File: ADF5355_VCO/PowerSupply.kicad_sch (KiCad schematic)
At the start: 14 parts, among them IC1 ADM7150ACPZ-3.3-R7, IC2 ADM7150ARDZ-5.0, J1 Conn_01x02, SW1 SW_SPST

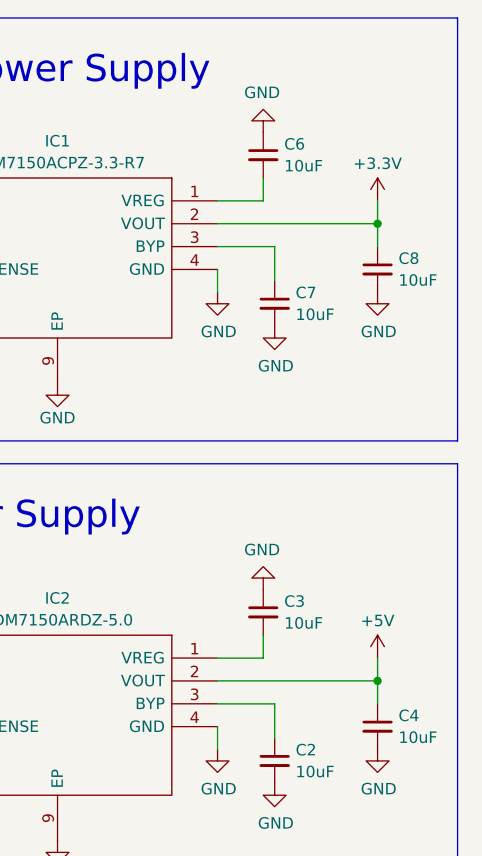
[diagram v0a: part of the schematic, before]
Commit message: Moved power ports to the main sheet
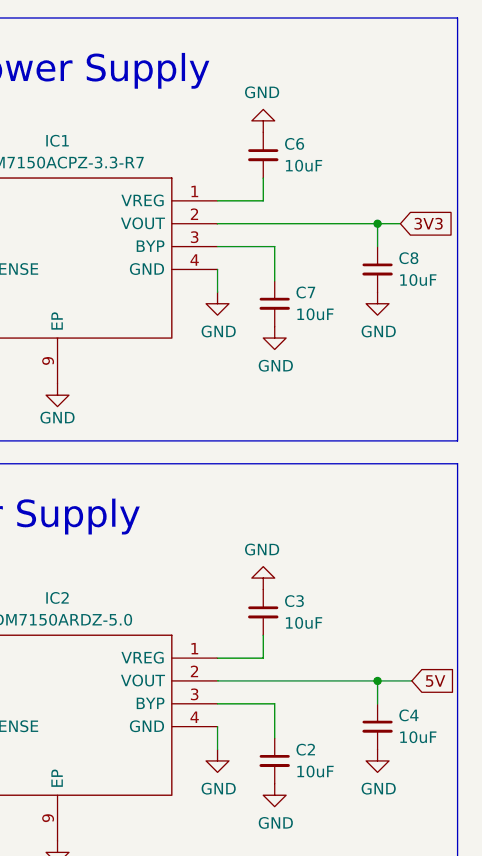
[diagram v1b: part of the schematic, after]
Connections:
- net +3.3V renamed 3V3
- net +5V renamed 5V
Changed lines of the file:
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@@
-    (stroke (width 0) (type default))
-  )
-  (wire (pts (xy 154.94 113.03) (xy 154.94 115.57))
     (stroke (width 0) (type default))
   )
@@
     (stroke (width 0) (type default))
   )
+  (wire (pts (xy 154.94 115.57) (xy 158.75 115.57))
+    (stroke (width 0) (type default))
+  )
+  (wire (pts (xy 154.94 64.77) (xy 157.48 64.77))
+    (stroke (width 0) (type default))
+  )
   (wire (pts (xy 137.16 62.23) (xy 142.24 62.23))
     (stroke (width 0) (type default))
@@
     (stroke (width 0) (type default))
   )
+  (wire (pts (xy 154.94 64.77) (xy 154.94 67.31))
+    (stroke (width 0) (type default))
+  )
   (wire (pts (xy 87.63 110.49) (xy 87.63 113.03))
     (stroke (width 0) (type default))
@@
   )
   (wire (pts (xy 101.6 120.65) (xy 95.25 120.65))
-    (stroke (width 0) (type default))
-  )
-  (wire (pts (xy 154.94 62.23) (xy 154.94 64.77))
-    (stroke (width 0) (type default))
-  )
-  (wire (pts (xy 154.94 64.77) (xy 154.94 67.31))
     (stroke (width 0) (type default))
   )
@@
   (text "External power" (at 39.37 77.47 0)
     (effects (font (size 3 3)) (justify left bottom))
+  )
+  (global_label "5V" (shape input) (at 158.75 115.57 0) (fields_autoplaced)
+    (effects (font (size 1.27 1.27)) (justify left))
+    (property "Intersheetrefs" "${INTERSHEET_REFS}" (at 163.2997 115.57 0)
+      (effects (font (size 1.27 1.27)) (justify left) hide)
+    )
+  )
+  (global_label "3V3" (shape input) (at 157.48 64.77 0) (fields_autoplaced)
+    (effects (font (size 1.27 1.27)) (justify left))
+    (property "Intersheetrefs" "${INTERSHEET_REFS}" (at 163.2392 64.77 0)
+      (effects (font (size 1.27 1.27)) (justify left) hide)
+    )
   )
   (global_label "DC_EN" (shape input) (at 101.6 64.77 180) (fields_autoplaced)
@@
         (path "/29349b68-071c-451b-9b1e-10b5ef7e12a6/00000000-0000-0000-0000-000064ac72b7"
           (reference "C7") (unit 1)
-        )
-      )
-    )
-  )
-  (symbol (lib_id "power:+5V") (at 154.94 113.03 0) (unit 1)
-    (in_bom yes) (on_board yes) (dnp no) (fields_autoplaced)
-    (property "Reference" "#PWR010" (at 154.94 116.84 0)
-      (effects (font (size 1.27 1.27)) hide)
-    )
-    (property "Value" "+5V" (at 154.94 108.8969 0)
-      (effects (font (size 1.27 1.27)))
-    )
-    (property "Footprint" "" (at 154.94 113.03 0)
-      (effects (font (size 1.27 1.27)) hide)
-    )
-    (property "Datasheet" "" (at 154.94 113.03 0)
-      (effects (font (size 1.27 1.27)) hide)
-    )
-    (pin "1")
-    (instances
-      (project "ADF5355_VCO"
-        (path "/29349b68-071c-451b-9b1e-10b5ef7e12a6/00000000-0000-0000-0000-000064ac72b7"
-          (reference "#PWR010") (unit 1)
         )
       )
@@
         )
       )
-    )
-  )
-  (symbol (lib_id "power:+3.3V") (at 154.94 62.23 0) (unit 1)
-    (in_bom yes) (on_board yes) (dnp no) (fields_autoplaced)
-    (property "Reference" "#PWR09" (at 154.94 66.04 0)
-      (effects (font (size 1.27 1.27)) hide)
-    )
-    (property "Value" "+3.3V" (at 154.94 58.0969 0)
-      (effects (font (size 1.27 1.27)))
-    )
-    (property "Footprint" "" (at 154.94 62.23 0)
-      (effects (font (size 1.27 1.27)) hide)
-    )
-    (property "Datasheet" "" (at 154.94 62.23 0)
-      (effects (font (size 1.27 1.27)) hide)
-    )
-    (pin "1")
-    (instances
-      (project "ADF5355_VCO"
-        (path "/29349b68-071c-451b-9b1e-10b5ef7e12a6/00000000-0000-0000-0000-000064ac72b7"
-          (reference "#PWR09") (unit 1)
-        )
-      )

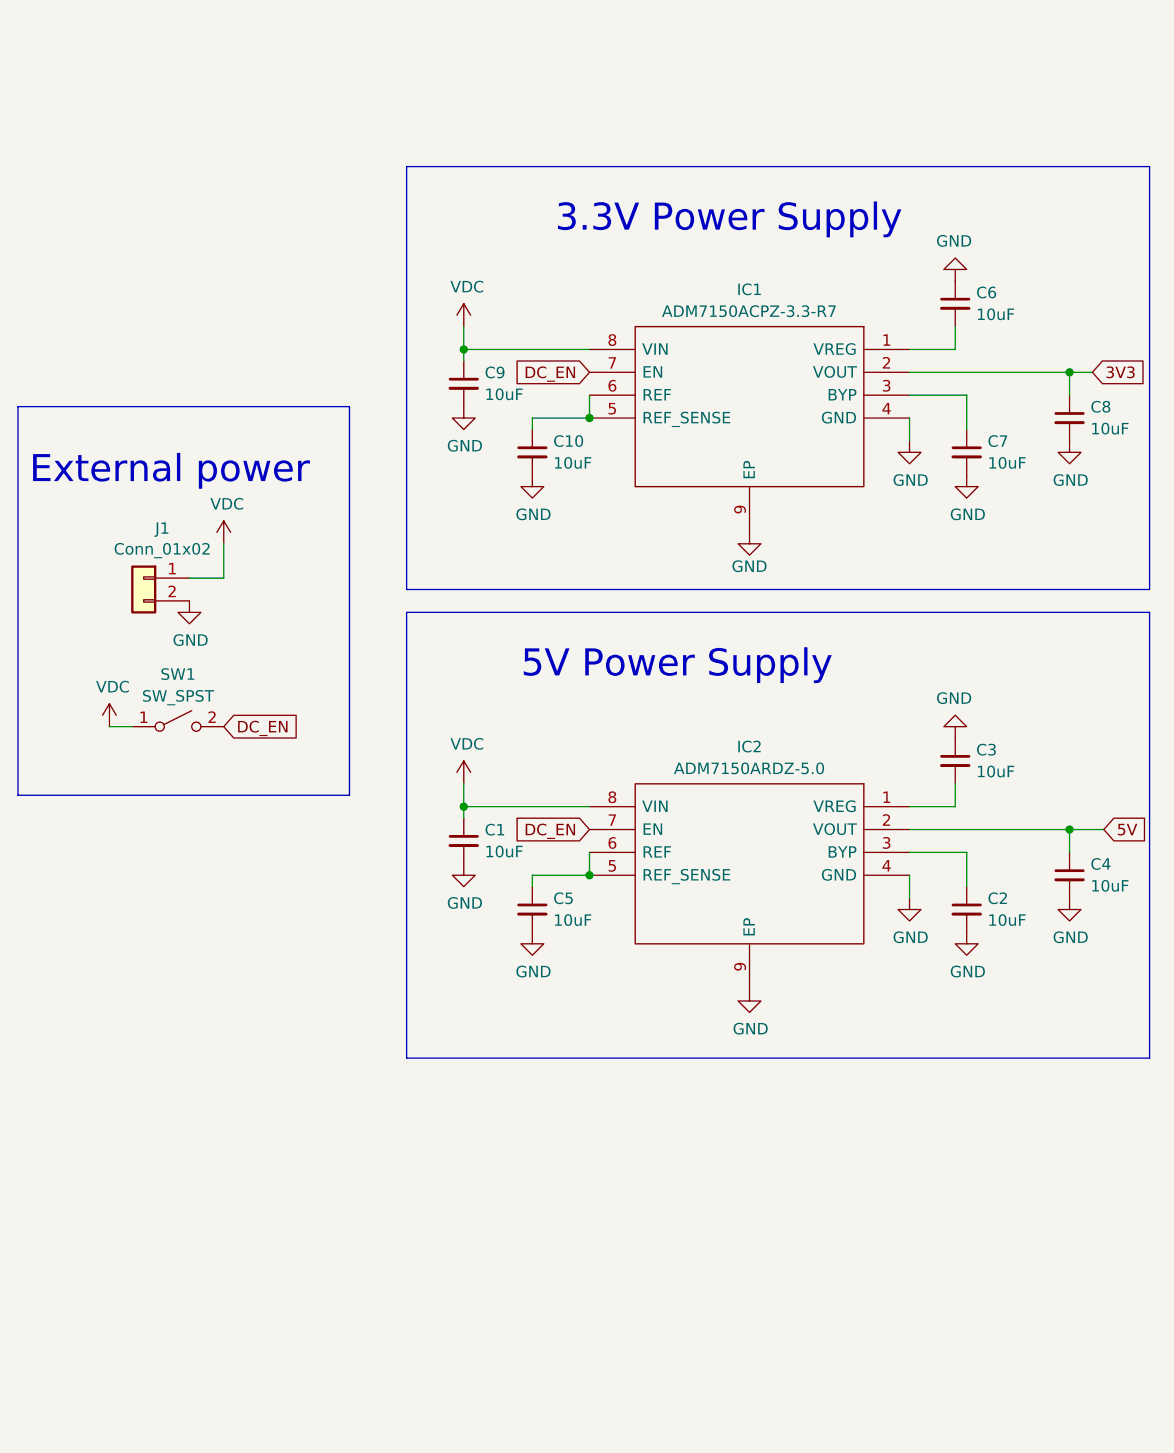
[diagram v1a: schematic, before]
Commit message: ¸Added USB connector and changed connections
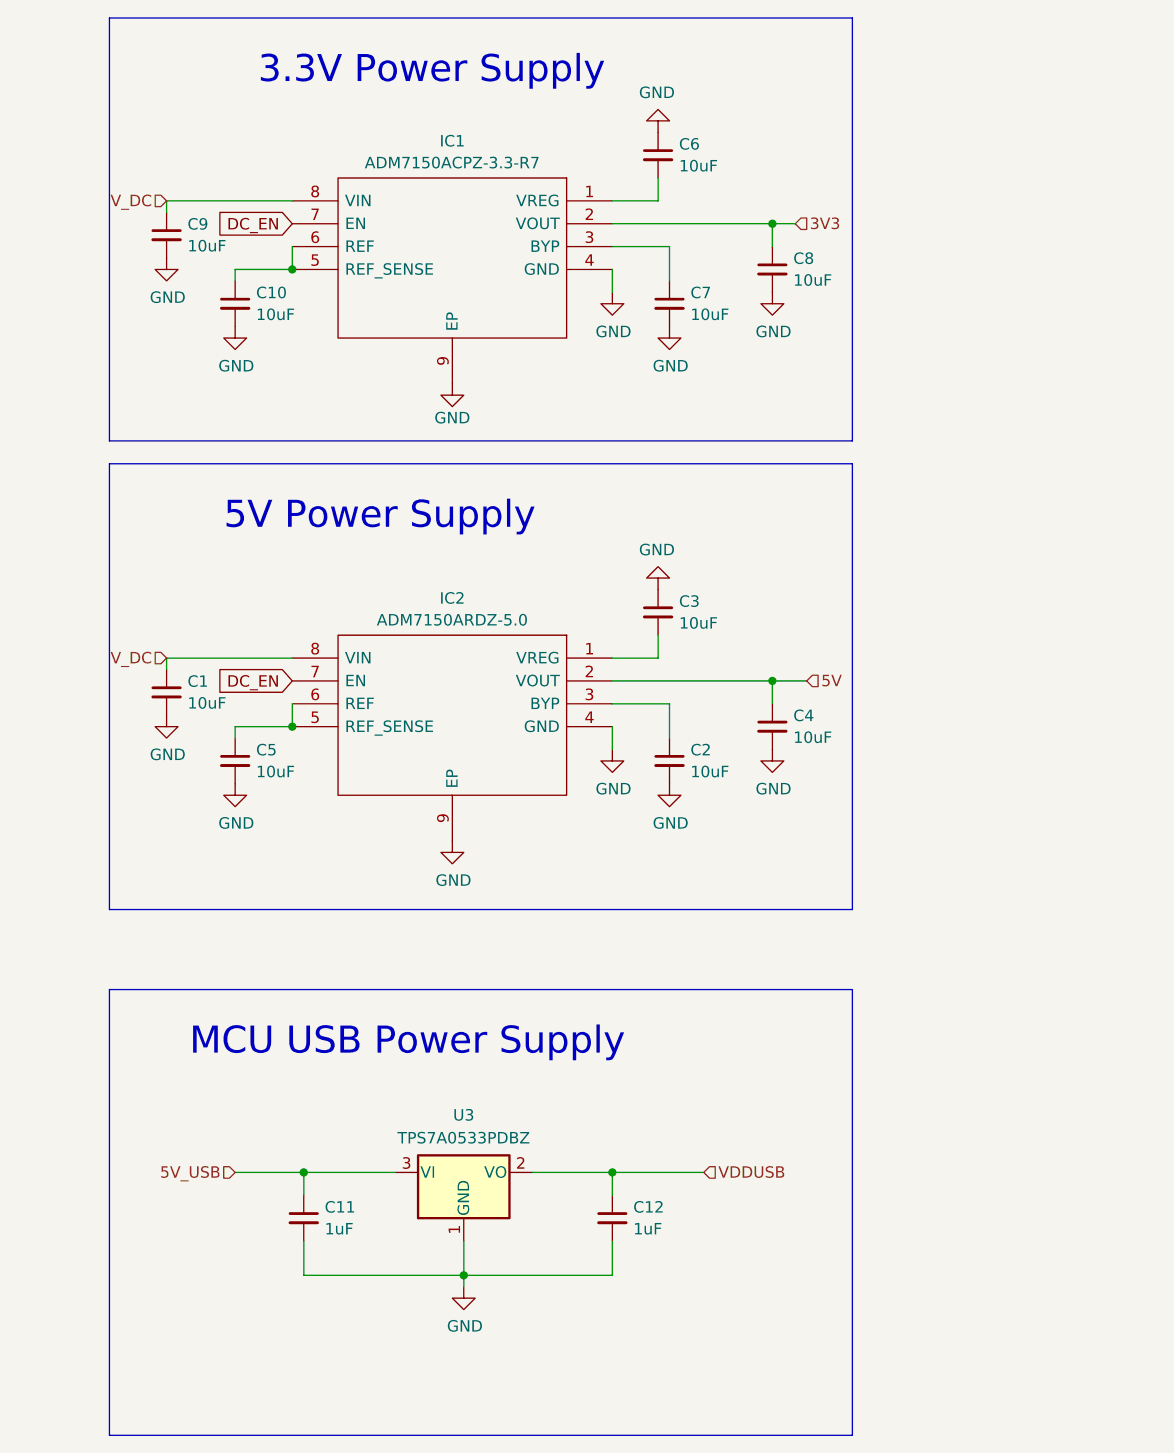
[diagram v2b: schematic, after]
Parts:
- removed J1: Conn_01x02, symbol Connector_Generic:Conn_01x02
- removed SW1: SW_SPST, symbol Switch:SW_SPST
- added C11, C12: 1uF, symbol Device:C_Small
- added U3: TPS7A0533PDBZ, Package_TO_SOT_SMD:SOT-23, symbol Regulator_Linear:TPS7A0533PDBZ
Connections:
- net GND: now also C11.2, C12.2, U3.1 (GND)
- net VDC renamed V_DC
- new net 5V_USB: C11.1, U3.3 (VI)
- new net VDDUSB: C12.1, U3.2 (VO)
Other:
- note added: "MCU USB Power Supply"
- note removed: "External power"
- moved on the sheet: C1, C10, C2, C3, C4, C5, C6, C7, C8, C9, IC1, IC2

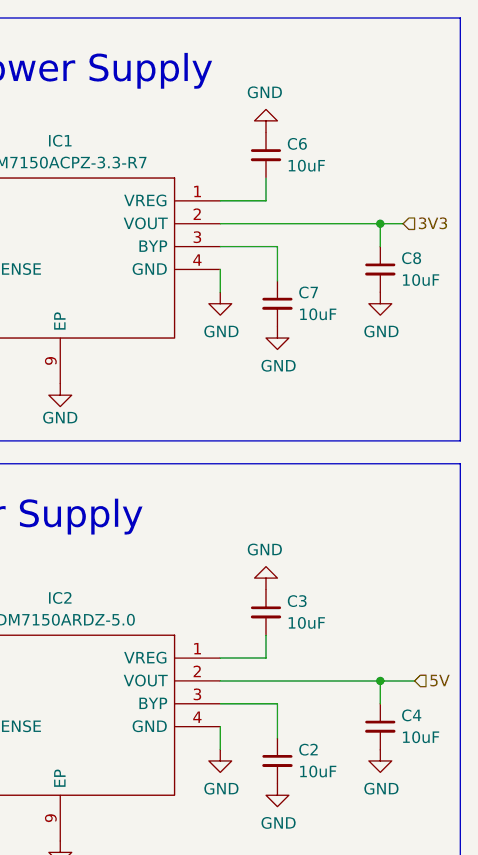
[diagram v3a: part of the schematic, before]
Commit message: Changed the power port
Changed all power ports to be global instead of them being hierarchical sheet pins
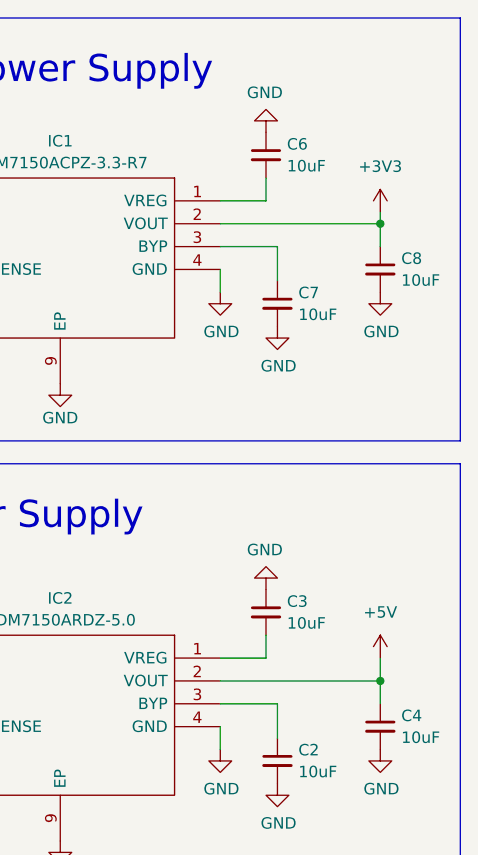
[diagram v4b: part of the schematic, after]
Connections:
- net 3V3 renamed +3V3
- net 5V renamed +5V
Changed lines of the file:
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@@
   (junction (at 68.58 104.14) (diameter 0) (color 0 0 0 0)
   )
+  (junction (at 121.92 48.26) (diameter 0) (color 0 0 0 0)
+  )
   (junction (at 87.63 165.1) (diameter 0) (color 0 0 0 0)
   )
   (junction (at 68.58 53.34) (diameter 0) (color 0 0 0 0)
   )
-  (junction (at 121.92 48.26) (diameter 0) (color 0 0 0 0)
-  )
   (junction (at 104.14 153.67) (diameter 0) (color 0 0 0 0)
   )
+  (junction (at 121.92 99.06) (diameter 0) (color 0 0 0 0)
+  )
   (junction (at 69.85 153.67) (diameter 0) (color 0 0 0 0)
   )
-  (junction (at 121.92 99.06) (diameter 0) (color 0 0 0 0)
-  )
   (wire (pts (xy 110.49 50.8) (xy 110.49 54.61))
     (stroke (width 0) (type default))
@@
     (stroke (width 0) (type default))
   )
+  (wire (pts (xy 121.92 46.99) (xy 121.92 48.26))
+    (stroke (width 0) (type default))
+  )
   (wire (pts (xy 54.61 45.72) (xy 54.61 46.99))
     (stroke (width 0) (type default))
@@
     (stroke (width 0) (type default))
   )
-  (wire (pts (xy 121.92 99.06) (xy 125.73 99.06))
-    (stroke (width 0) (type default))
-  )
-  (wire (pts (xy 121.92 48.26) (xy 124.46 48.26))
-    (stroke (width 0) (type default))
-  )
   (wire (pts (xy 104.14 165.1) (xy 87.63 165.1))
     (stroke (width 0) (type default))
@@
   )
   (wire (pts (xy 109.22 96.52) (xy 109.22 93.98))
+    (stroke (width 0) (type default))
+  )
+  (wire (pts (xy 121.92 96.52) (xy 121.92 99.06))
     (stroke (width 0) (type default))
   )
@@
     (effects (font (size 1.27 1.27)) (justify right))
   )
-  (hierarchical_label "3V3" (shape input) (at 124.46 48.26 0) (fields_autoplaced)
-    (effects (font (size 1.27 1.27)) (justify left))
-  )
-  (hierarchical_label "5V" (shape input) (at 125.73 99.06 0) (fields_autoplaced)
-    (effects (font (size 1.27 1.27)) (justify left))
-  )
   (hierarchical_label "V_DC" (shape input) (at 54.61 45.72 180) (fields_autoplaced)
     (effects (font (size 1.27 1.27)) (justify right))
@@
     )
     (pin "1")
-    (pin "2")
     (pin "3")
     (pin "4")
@@
     (pin "8")
     (pin "9")
+    (pin "2")
     (instances
       (project "ADF5355_VCO"
@@
     )
   )
+  (symbol (lib_id "power:+3V3") (at 121.92 46.99 0) (unit 1)
+    (in_bom yes) (on_board yes) (dnp no) (fields_autoplaced)
+    (property "Reference" "#PWR027" (at 121.92 50.8 0)
+      (effects (font (size 1.27 1.27)) hide)
+    )
+    (property "Value" "+3V3" (at 121.92 41.91 0)
+      (effects (font (size 1.27 1.27)))
+    )
+    (property "Footprint" "" (at 121.92 46.99 0)
+      (effects (font (size 1.27 1.27)) hide)
+    )
+    (property "Datasheet" "" (at 121.92 46.99 0)
+      (effects (font (size 1.27 1.27)) hide)
+    )
+    (pin "1")
+    (instances
+      (project "ADF5355_VCO"
+        (path "/29349b68-071c-451b-9b1e-10b5ef7e12a6/00000000-0000-0000-0000-000064ac72b7"
+          (reference "#PWR027") (unit 1)
+        )
+      )
+    )
+  )
   (symbol (lib_id "Device:C_Small") (at 110.49 107.95 0) (unit 1)
     (in_bom yes) (on_board yes) (dnp no) (fields_autoplaced)
@@
     )
     (pin "1")
-    (pin "2")
     (pin "3")
     (pin "4")
@@
     (pin "8")
     (pin "9")
+    (pin "2")
     (instances
       (project "ADF5355_VCO"
@@
         )
       )
+    )
+  )
+  (symbol (lib_id "power:+5V") (at 121.92 96.52 0) (unit 1)
+    (in_bom yes) (on_board yes) (dnp no) (fields_autoplaced)
+    (property "Reference" "#PWR039" (at 121.92 100.33 0)
+      (effects (font (size 1.27 1.27)) hide)
+    )
+    (property "Value" "+5V" (at 121.92 91.44 0)
+      (effects (font (size 1.27 1.27)))
+    )
+    (property "Footprint" "" (at 121.92 96.52 0)
+      (effects (font (size 1.27 1.27)) hide)
+    )
+    (property "Datasheet" "" (at 121.92 96.52 0)
+      (effects (font (size 1.27 1.27)) hide)
+    )
+    (pin "1")
+    (instances
+      (project "ADF5355_VCO"
+        (path "/29349b68-071c-451b-9b1e-10b5ef7e12a6/00000000-0000-0000-0000-000064ac72b7"
+          (reference "#PWR039") (unit 1)
+        )
+      )
